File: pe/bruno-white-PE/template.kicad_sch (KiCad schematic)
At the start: 8 parts, among them Q1 NMOS, U1 XL1509-ADJ

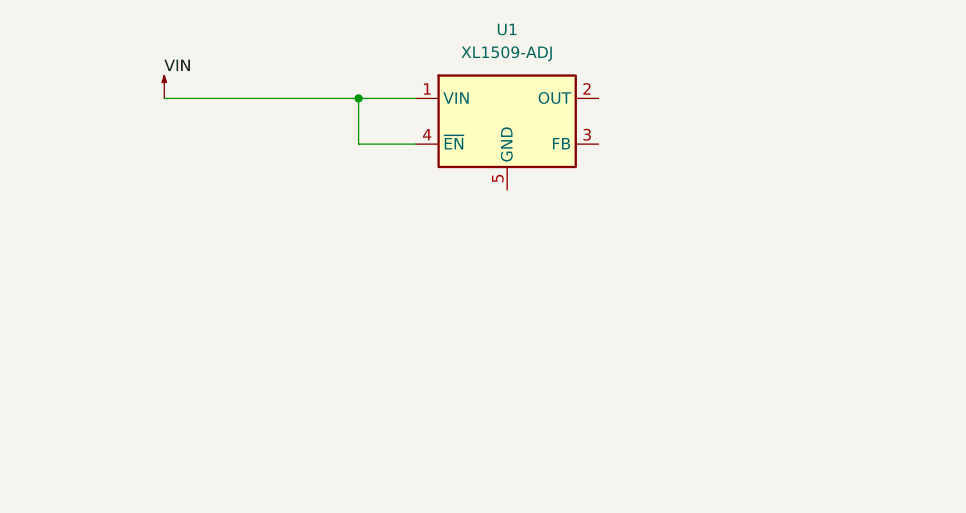
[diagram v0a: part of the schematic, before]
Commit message: LV and PE
I adjusted the wheatstone bridge circuit in my schematic, but I still have lots to do for that. Then for my PE buck converter I asked Edmund for some help and then I used the datasheet of the Buck DC DC converter to realize that it has a power transistor. So I added some components to that converter, but now I don't know what to do with the feedback.
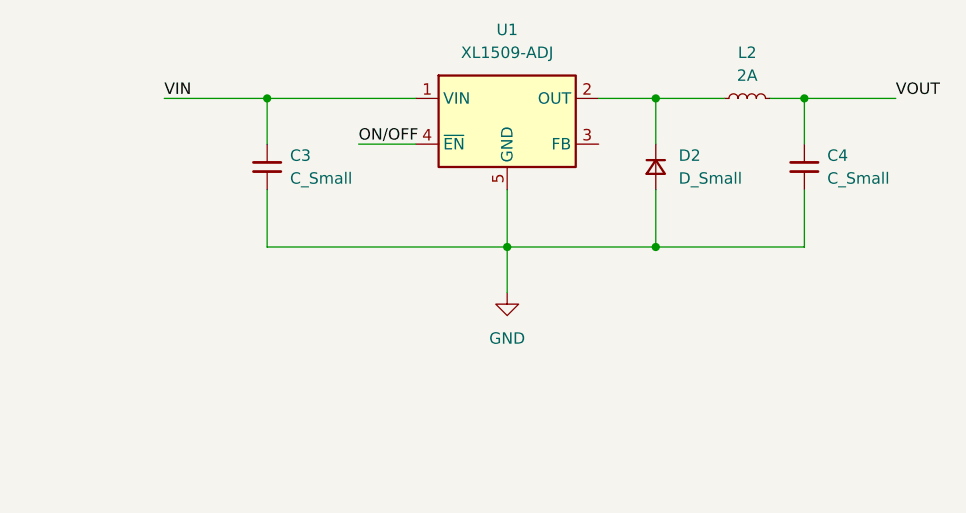
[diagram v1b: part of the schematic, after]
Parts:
- added C3: C_Small, symbol Device:C_Small
- added C4: C_Small, Package_SO:SOIC-8_3.9x4.9mm_P1.27mm, symbol Device:C_Small
- added D2: D_Small, symbol Device:D_Small
- added L2: 2A, Relay_THT:Relay_DPDT_Finder_30.22, symbol Device:L_Small
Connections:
- net GND: now also U1.5 (GND), U1.6 (GND), U1.7 (GND), U1.8 (GND), C3.2, C4.2, D2.2 (A)
- net VIN: now also U1.1 (VIN), C3.1
- net VOUT: now also C4.1, L2.2
- net ON/OFF: now reaches U1.4 (~{EN})
- net ON/OFF: no longer U1.1 (VIN)
- net at U1.2 (OUT): now also D2.1 (K), L2.1

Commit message: LV and PE edits
Assigned footprints to my strain gauge to make a PCB design, but then apparently they aren't connected so I need to fix that... I gave up on my strain gauge pcb and then for PE I was just messing around with the PCB design which worked for my buck converter. I have also added the link to my google docs!!!
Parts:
- C1, C2, C4: footprint Package_SO:SOIC-8_3.9x4.9mm_P1.27mm -> Capacitor_SMD:C_0603_1608Metric_Pad1.08x0.95mm_HandSolder
- C3: footprint (none) -> Capacitor_SMD:C_0603_1608Metric_Pad1.08x0.95mm_HandSolder
- D1, D2: footprint (none) -> Diode_SMD:D_0603_1608Metric_Pad1.05x0.95mm_HandSolder
- L1, L2: footprint Relay_THT:Relay_DPDT_Finder_30.22 -> Inductor_SMD:L_0603_1608Metric_Pad1.05x0.95mm_HandSolder
- R1: footprint (none) -> Resistor_SMD:R_0603_1608Metric_Pad0.98x0.95mm_HandSolder
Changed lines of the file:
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@@
 			)
 		)
-		(property "Footprint" "Relay_THT:Relay_DPDT_Finder_30.22"
+		(property "Footprint" "Inductor_SMD:L_0603_1608Metric_Pad1.05x0.95mm_HandSolder"
 			(at 167.64 69.85 0)
 			(hide yes)
@@
 			)
 		)
-		(property "Footprint" ""
+		(property "Footprint" "Capacitor_SMD:C_0603_1608Metric_Pad1.08x0.95mm_HandSolder"
 			(at 114.3 77.47 0)
 			(hide yes)
@@
 			)
 		)
-		(property "Footprint" "Package_SO:SOIC-8_3.9x4.9mm_P1.27mm"
+		(property "Footprint" "Capacitor_SMD:C_0603_1608Metric_Pad1.08x0.95mm_HandSolder"
 			(at 173.99 77.47 0)
 			(hide yes)
@@
 			)
 		)
-		(property "Footprint" "Relay_THT:Relay_DPDT_Finder_30.22"
+		(property "Footprint" "Inductor_SMD:L_0603_1608Metric_Pad1.05x0.95mm_HandSolder"
 			(at 85.09 166.37 0)
 			(hide yes)
@@
 			)
 		)
-		(property "Footprint" ""
+		(property "Footprint" "Diode_SMD:D_0603_1608Metric_Pad1.05x0.95mm_HandSolder"
 			(at 77.47 176.53 90)
 			(hide yes)
@@
 			)
 		)
-		(property "Footprint" ""
+		(property "Footprint" "Diode_SMD:D_0603_1608Metric_Pad1.05x0.95mm_HandSolder"
 			(at 157.48 77.47 90)
 			(hide yes)
@@
 			)
 		)
-		(property "Footprint" ""
+		(property "Footprint" "Resistor_SMD:R_0603_1608Metric_Pad0.98x0.95mm_HandSolder"
 			(at 104.14 176.53 0)
 			(hide yes)
@@
 			)
 		)
-		(property "Footprint" "Package_SO:SOIC-8_3.9x4.9mm_P1.27mm"
+		(property "Footprint" "Capacitor_SMD:C_0603_1608Metric_Pad1.08x0.95mm_HandSolder"
 			(at 91.44 176.53 0)
 			(hide yes)
@@
 			)
 		)
-		(property "Footprint" "Package_SO:SOIC-8_3.9x4.9mm_P1.27mm"
+		(property "Footprint" "Capacitor_SMD:C_0603_1608Metric_Pad1.08x0.95mm_HandSolder"
 			(at 49.53 176.53 0)
 			(hide yes)

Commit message: Power Electronics DONE
This was my last adjustment for today to my buck converter schematic. I added a resistor to the output voltage and connected feedback to it. I'm not too sure how I was supposed to connect feedback because it was kind of stuck in the middle of everything... I have also uploaded all my PE notes on the google doc in the initial learning tab. Thank you so much!
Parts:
- added R2: R_Small, Package_DIP:DIP-8_W7.62mm, symbol Device:R_Small
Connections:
- net GND: now also U1.3 (FB), R2.2
- net VOUT: now also R2.1
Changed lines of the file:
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@@
+	)
+	(junction
+		(at 173.99 86.36)
+		(diameter 0)
+		(color 0 0 0 0)
 	)
 	(junction
@@
 	)
 	(junction
+		(at 151.13 86.36)
+		(diameter 0)
+		(color 0 0 0 0)
+	)
+	(junction
 		(at 91.44 166.37)
 		(diameter 0)
@@
 	(wire
 		(pts
-			(xy 140.97 86.36) (xy 173.99 86.36)
+			(xy 140.97 86.36) (xy 151.13 86.36)
+		)
+		(stroke
+			(width 0)
+			(type default)
+		)
+	)
+	(wire
+		(pts
+			(xy 185.42 74.93) (xy 185.42 69.85)
 		)
 		(stroke
@@
 	(wire
 		(pts
+			(xy 151.13 86.36) (xy 173.99 86.36)
+		)
+		(stroke
+			(width 0)
+			(type default)
+		)
+	)
+	(wire
+		(pts
 			(xy 157.48 69.85) (xy 157.48 74.93)
 		)
@@
 	(wire
 		(pts
+			(xy 173.99 69.85) (xy 185.42 69.85)
+		)
+		(stroke
+			(width 0)
+			(type default)
+		)
+	)
+	(wire
+		(pts
 			(xy 49.53 179.07) (xy 49.53 185.42)
 		)
@@
 	(wire
 		(pts
-			(xy 173.99 69.85) (xy 184.15 69.85)
+			(xy 173.99 86.36) (xy 185.42 86.36)
 		)
 		(stroke
@@
 	(wire
 		(pts
+			(xy 151.13 74.93) (xy 151.13 86.36)
+		)
+		(stroke
+			(width 0)
+			(type default)
+		)
+	)
+	(wire
+		(pts
 			(xy 140.97 86.36) (xy 140.97 91.44)
 		)
@@
 		(pts
 			(xy 114.3 86.36) (xy 114.3 80.01)
+		)
+		(stroke
+			(width 0)
+			(type default)
+		)
+	)
+	(wire
+		(pts
+			(xy 185.42 80.01) (xy 185.42 86.36)
 		)
 		(stroke
@@
 					(unit 1)
 				)
+			)
+		)
+	)
+	(symbol
+		(lib_id "Device:R_Small")
+		(at 185.42 77.47 0)
+		(unit 1)
+		(body_style 1)
+		(exclude_from_sim no)
+		(in_bom yes)
+		(on_board yes)
+		(in_pos_files yes)
+		(dnp no)
+		(fields_autoplaced yes)
+		(property "Reference" "R2"
+			(at 187.96 76.1999 0)
+			(show_name no)
+			(do_not_autoplace no)
+			(effects
+				(font
+					(size 1.016 1.016)
+				)
+				(justify left)
+			)
+		)
+		(property "Value" "R_Small"
+			(at 187.96 78.7399 0)
+			(show_name no)
+			(do_not_autoplace no)
+			(effects
+				(font
+					(size 1.27 1.27)
+				)
+				(justify left)
+			)
+		)
+		(property "Footprint" "Package_DIP:DIP-8_W7.62mm"
+			(at 185.42 77.47 0)
+			(hide yes)
+			(show_name no)
+			(do_not_autoplace no)
+			(effects
+				(font
+					(size 1.27 1.27)
+				)
+			)
+		)
+		(property "Datasheet" ""
+			(at 185.42 77.47 0)
+			(hide yes)
+			(show_name no)
+			(do_not_autoplace no)
+			(effects
+				(font
+					(size 1.27 1.27)
+				)
+			)
+		)
+		(property "Description" "Resistor, small symbol"
+			(at 185.42 77.47 0)
+			(hide yes)
+			(show_name no)
+			(do_not_autoplace no)
+			(effects
+				(font
+					(size 1.27 1.27)
+				)
+			)
+		)
+		(pin "1"
+		)
+		(pin "2"
+		)
+		(instances
+			(project "template"
+				(path "/e994741c-7c7d-4124-9d00-43b883baa61d"
+					(reference "R2")
+					(unit 1)
+				)
